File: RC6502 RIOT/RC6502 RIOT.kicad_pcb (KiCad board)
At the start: 2 copper layers, 99.1 x 69.2 mm, 45 parts, among them J1 Audio, J2 VDU_BASE, J3 P, J8 Composite, J9 RC6502_Backplane_Extra, U1 TIA_NTSC, U2 74HCT138, U3 VDU_Port, X1 3.579545 MHz

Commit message: RIOT module layout done
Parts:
- removed C10, C9: 470pF, Capacitors_THT:C_Disc_D4.7mm_W2.5mm_P5.00mm
- removed C11: 820pF, Capacitors_THT:C_Disc_D4.7mm_W2.5mm_P5.00mm
- removed C12: 100nF, Capacitors_THT:C_Disc_D4.7mm_W2.5mm_P5.00mm
- removed C5, C6: 68nF, Capacitors_THT:C_Disc_D4.7mm_W2.5mm_P5.00mm
- removed C7: 22pF, Capacitors_THT:C_Disc_D4.7mm_W2.5mm_P5.00mm
- removed C8: 47pF, Capacitors_THT:C_Disc_D4.7mm_W2.5mm_P5.00mm
- removed J8: Composite, RCA:rca_yellow
- removed R10: 6k8, Resistors_THT:R_Axial_DIN0207_L6.3mm_D2.5mm_P10.16mm_Horizontal
- removed R11, R12, R9: 1k, Resistors_THT:R_Axial_DIN0207_L6.3mm_D2.5mm_P10.16mm_Horizontal
- removed R13: 18k, Resistors_THT:R_Axial_DIN0207_L6.3mm_D2.5mm_P10.16mm_Horizontal
- removed R14: 9k1, Resistors_THT:R_Axial_DIN0207_L6.3mm_D2.5mm_P10.16mm_Horizontal
- removed R15, R16: 220, Resistors_THT:R_Axial_DIN0207_L6.3mm_D2.5mm_P10.16mm_Horizontal
- removed R17, R18: 10k, Resistors_THT:R_Axial_DIN0207_L6.3mm_D2.5mm_P10.16mm_Horizontal
- removed R2, R4, R6, R8: 3K3, Resistors_THT:R_Axial_DIN0207_L6.3mm_D2.5mm_P10.16mm_Horizontal
- removed R3: 56k, Resistors_THT:R_Axial_DIN0207_L6.3mm_D2.5mm_P10.16mm_Horizontal
- removed R5: 27K, Resistors_THT:R_Axial_DIN0207_L6.3mm_D2.5mm_P10.16mm_Horizontal
- removed R7: 110k, Resistors_THT:R_Axial_DIN0207_L6.3mm_D2.5mm_P10.16mm_Horizontal
- removed RV1: 500k, Potentiometers:Potentiometer_Trimmer_Bourns_3296W
- removed U3: VDU_Port, vdu_amplifier:Amplifier
- removed X1: 3.579545 MHz, Oscillator:Oscillator_DIP-14
- added J4: RIGHT PLAYER, RND_DSUB:DSUB-9_Male_Vertical_Pitch2.77x2.84mm, F.Cu at (143.5, 128.9)
- added J5: AUX, Pin_Headers:Pin_Header_Straight_1x03_Pitch2.54mm, F.Cu at (54.6, 117.5)
- added JP10: R_DIFF, Pin_Headers:Pin_Header_Straight_1x03_Pitch2.54mm, F.Cu at (108.6, 76.8)
- added JP11: RAM_EN, Pin_Headers:Pin_Header_Straight_1x03_Pitch2.54mm, F.Cu at (108.6, 121.3)
- added JP6: RAM_SEL, Pin_Headers:Pin_Header_Straight_1x03_Pitch2.54mm, F.Cu at (108.6, 132.7)
- added JP7: IRQ_SEL, Pin_Headers:Pin_Header_Straight_1x03_Pitch2.54mm, F.Cu at (95.9, 121.3)
- added JP8: B/W, Pin_Headers:Pin_Header_Straight_1x03_Pitch2.54mm, F.Cu at (84.5, 76.8)
- added JP9: L_DIFF, Pin_Headers:Pin_Header_Straight_1x03_Pitch2.54mm, F.Cu at (96.5, 76.8)
- added SW1: SELECT, Buttons_Switches_THT:SW_PUSH_6mm, F.Cu at (117.5, 76.8)
- added SW2: START, Buttons_Switches_THT:SW_PUSH_6mm, F.Cu at (128.3, 76.8)
- C3, C4: value 68nF -> 1nF
- J1: value Audio -> LEFT PLAYER; footprint RCA:rca_yellow -> RND_DSUB:DSUB-9_Male_Vertical_Pitch2.77x2.84mm
- J3: value P -> Analog
- JP1: value CADJ -> IRQ_EN; footprint Pin_Headers:Pin_Header_Straight_1x02_Pitch2.54mm -> Pin_Headers:Pin_Header_Straight_1x03_Pitch2.54mm
- JP2: value CS0_SEL -> CS1_SEL
- JP3: value CS3_SEL -> CS2_SEL
- R1: value 27k -> 3k3
- U1: value TIA_NTSC -> RIOT
- moved JP4 64.7 mm to (70.5, 138.4), turned to 90 degrees
- moved JP5 64.5 mm to (61.6, 138.4), turned to 90 degrees
- moved JP2 49.1 mm to (83.2, 132.7), turned to 90 degrees
- moved JP1 43.3 mm to (83.2, 121.3), turned to 90 degrees
- moved C4 40.6 mm to (54.6, 112.4)
- moved C3 35.9 mm to (54.6, 102.2)
- moved JP3 33.4 mm to (95.9, 132.7), turned to 90 degrees
- moved R1 21.6 mm to (103.5, 111.8), turned to 180 degrees
- moved J2 13.3 mm to (132.7, 117.5)
- moved C2 13.3 mm to (126.4, 111.1)
- moved U2 13.3 mm to (120.0, 114.9)
- moved J1 5.46 mm to (143.5, 96.5)
- moved J3 5.24 mm to (70.5, 76.8)
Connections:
- C3 pad 1: GND -> /PA0
- C3 pad 2: /P0 -> GND
- C4 pad 1: GND -> /PB0
- C4 pad 2: /P1 -> GND
- J1 pad 1: GND -> /PA4
- J1 pad 2: Net-(J1-Pad2) -> /PA5
- J2 pad 10: TIA_BASE -> RIOT_BASE
- J2 pad 12: TIA_BASE -> RIOT_BASE
- J2 pad 14: TIA_BASE -> RIOT_BASE
- J2 pad 2: TIA_BASE -> RIOT_BASE
- J2 pad 4: TIA_BASE -> RIOT_BASE
- J2 pad 6: TIA_BASE -> RIOT_BASE
- J2 pad 8: TIA_BASE -> RIOT_BASE
- J9 pad 10: (no net) -> /A6
- J9 pad 20: (no net) -> /~RES
- J9 pad 21: /PHI0 -> (no net)
- J9 pad 22: (no net) -> /IRQ_IN
- J9 pad 25: /RDY -> (no net)
- J9 pad 37: (no net) -> /NMI_IN
- J9 pad 5: (no net) -> /A11
- J9 pad 7: (no net) -> /A9
- JP1 pad 2: /CADJ -> /~IRQ
- JP2 pad 1: /A12 -> /A7
- JP2 pad 2: /~CS0 -> /CS1
- JP2 pad 3: TIA_BASE -> VCC
- JP3 pad 1: /A7 -> /A12
- JP3 pad 2: /~CS3 -> /~CS2
- JP3 pad 3: GND -> RIOT_BASE
- JP4 pad 1: /T1_IN -> /T1
- JP5 pad 1: /T0_IN -> /T0
- R1 pad 1: /CSYNC -> VCC
- R1 pad 2: VIDEO -> Net-(JP1-Pad1)
- U1 pad 10: /CADJ -> /PA2
- U1 pad 11: /OSC_IN -> /PA3
- U1 pad 12: /AUD0 -> /PA4
- U1 pad 13: /AUD0 -> /PA5
- U1 pad 14: /D0 -> /PA6
- U1 pad 15: /D1 -> /PA7
- U1 pad 16: /D2 -> /PB7
- U1 pad 17: /D3 -> /PB6
- U1 pad 18: /D4 -> /PB5
- U1 pad 19: /D5 -> /PB4
- U1 pad 2: /CSYNC -> /A5
- U1 pad 21: /~CS3 -> /PB3
- U1 pad 22: GND -> /PB2
- U1 pad 23: VCC -> /PB1
- U1 pad 24: /~CS0 -> /PB0
- U1 pad 25: /R/~W -> /~IRQ
- U1 pad 26: /PHI2 -> /D7
- U1 pad 27: /A5 -> /D6
- U1 pad 28: /A4 -> /D5
- U1 pad 29: /A3 -> /D4
- U1 pad 3: /RDY -> /A4
- U1 pad 30: /A2 -> /D3
- U1 pad 31: /A1 -> /D2
- U1 pad 32: /A0 -> /D1
- U1 pad 33: /D6 -> /D0
- U1 pad 34: /D7 -> /~RES
- U1 pad 35: /T1 -> /R/~W
- U1 pad 36: /T0 -> /~RS
- U1 pad 37: /P3 -> /~CS2
- U1 pad 38: /P2 -> /CS1
- U1 pad 39: /P1 -> /PHI2
- U1 pad 4: /PHI0 -> /A3
- U1 pad 40: /P0 -> /A6
- U1 pad 5: /LUM1 -> /A2
- U1 pad 6: (no net) -> /A1
- U1 pad 7: /LUM2 -> /A0
- U1 pad 8: /LUM0 -> /PA0
- U1 pad 9: /COLOR -> /PA1
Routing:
- net VCC: track 470.4 -> 245.1 mm, vias 10 -> 5
- net /PB0: track 0.00 -> 137.5 mm, vias 0 -> 2
- net /A6: track 0.00 -> 126.6 mm, vias 0 -> 4
- net /PA0: track 0.00 -> 113.3 mm, vias 0 -> 3
- net /PA7: track 0.00 -> 112.9 mm, vias 0 -> 3
- net /PB1: track 0.00 -> 110.5 mm
- net /PA6: track 0.00 -> 108.1 mm, vias 0 -> 3
- net /PA1: track 0.00 -> 106.1 mm, vias 0 -> 3
- net /PA2: track 0.00 -> 105.2 mm, vias 0 -> 3
- net /P1: track 22.2 -> 126.7 mm, vias 0 -> 2
- net /PA3: track 0.00 -> 103.9 mm, vias 0 -> 1
- net /PA5: track 0.00 -> 103.6 mm, vias 0 -> 3
- net /P0: track 20.5 -> 123.7 mm, vias 0 -> 2
- net /PA4: track 0.00 -> 98.5 mm, vias 0 -> 1
- net Net-(J9-Pad38): track 106.8 -> 10.6 mm, vias 4 -> 0
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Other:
- outline, holes or cut-outs redrawn
- board text added: "$80 $280"
- board text added: "$ADR"
- board text added: "+ $0 + $1 + $2 + $3 + $4 + $14 + $15 + $16 + $17"
- board text added: "1-2 Disabled 2-3 Enabled"
- board text added: "1-2 ~IRQ 2-3 ~NMI"
- board text added: "6532"
- board text added: "Atari 2600"
- board text added: "B/W COLOR"
- board text added: "BASE"
- board text added: "CS1"
- board text added: "Description"
- board text added: "IRQ_EN"
- board text added: "IRQ_SEL"
- board text added: "LEFT DIFFICULTY"
- board text added: "Port A data register (joysticks...) Port A data direction register (DDR) Port B data (console switches) Port B DDR Timer output Set 1 clock interval Set 8 clock interval Set 64 clock interval Set 1024 clock interval"
- board text added: "RAM I/O TIMER (RIOT) 6532"
- board text added: "RAM Registers"
- board text added: "RC6502"
- board text added: "RC6502 RIOT 2600 Revision A"
- board text added: "RIGHT DIFFICULTY"
- board text added: "RIOT BASE"
- board text added: "RIOT_BASE RIOT_BASE + $800"
- board text added: "Swcha Swacnt Swchb Swbcnt Intim Tim1t Tim8t Tim64t T1024t"
- board text added: "Symbol"
- board text added: "~CS2"
- board text added: "~RAM_EN"
- board text added: "~RAM_SEL"
- board text removed: "2x 470pF"
- board text removed: "2x 68nF"
- board text removed: "3.579545 MHz"
- board text removed: "ANALOG INPUT"
- board text removed: "AUDIO"
- board text removed: "BUS EN"
- board text removed: "CO10444"
- board text removed: "COLOR DELAY ADJUST"
- board text removed: "Composite Video Amplifier"
- board text removed: "NTSC Oscillator"
- board text removed: "RC6502 TIA (NTSC) Revision A"
- board text removed: "T0"
- board text removed: "T1"
- board text removed: "Television Interface Adapter (TIA) CO10444"
- board text removed: "VDU BASE"
- board text removed: "VIDEO"
- board text removed: "~CS0"
- board text removed: "~CS3"

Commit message: Updated gerbers for order
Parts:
- moved J3 5.08 mm to (75.6, 76.8)
- moved JP8 1.27 mm to (83.2, 76.8)
- moved SW1 0.64 mm to (118.1, 76.8)
- moved JP9 0.63 mm to (95.9, 76.8)
- moved SW2 0.63 mm to (128.9, 76.8)
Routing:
- net /P3: track 90.2 -> 85.1 mm
- net /P2: track 83.9 -> 78.8 mm
- net /P1: track 126.7 -> 121.6 mm
- net /P0: track 123.7 -> 118.6 mm
- net /PB0: track 137.5 -> 139.2 mm
- net /PB1: track 110.5 -> 111.8 mm
- net /PB3: track 83.9 -> 82.6 mm
- net /PB6: track 85.4 -> 84.8 mm
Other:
- board text added: "T0"
- board text added: "T1"

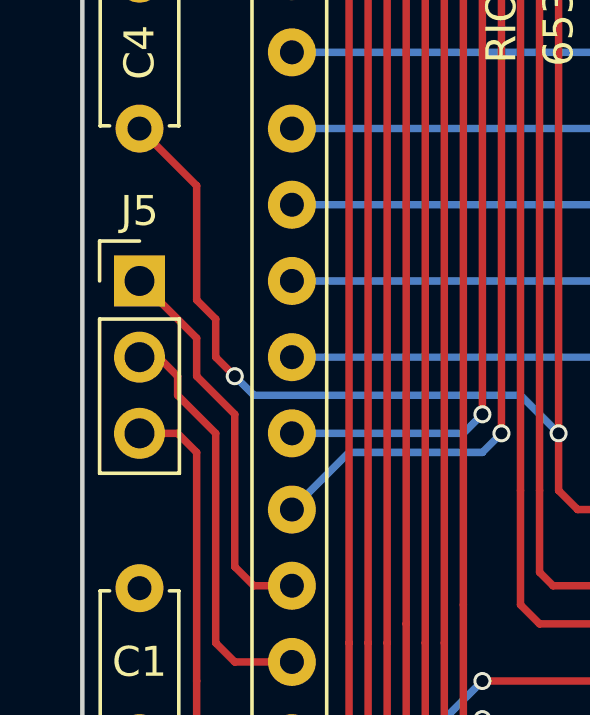
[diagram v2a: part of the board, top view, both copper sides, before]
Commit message: Added silkscreen markings for AUX header
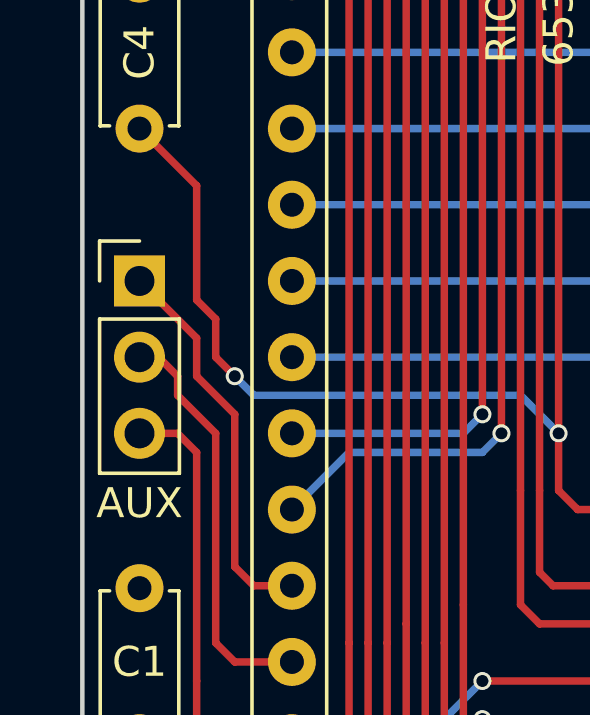
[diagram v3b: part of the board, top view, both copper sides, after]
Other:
- board text added: "AUX"
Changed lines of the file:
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@@
     (links 103)
     (no_connects 0)
-    (area 49.19 44.45 153.84 156.924763)
+    (area 52.629999 74.854999 151.840001 144.220001)
     (thickness 1.6)
-    (drawings 139)
+    (drawings 143)
     (tracks 1120)
     (zones 0)
@@
     (descr "Through hole straight pin header, 1x03, 2.54mm pitch, single row")
     (tags "Through hole pin header THT 1x03 2.54mm single row")
-    (fp_text reference J5 (at 0 -2.33) (layer F.SilkS)
-      (effects (font (size 1 1) (thickness 0.15)))
-    )
-    (fp_text value AUX (at 0 7.41) (layer F.Fab)
+    (fp_text reference J5 (at 0 -2.33) (layer F.Fab)
+      (effects (font (size 1 1) (thickness 0.15)))
+    )
+    (fp_text value AUX (at 0 7.41) (layer F.SilkS)
       (effects (font (size 1 1) (thickness 0.15)))
     )
@@
     )
   )
+  (gr_text AUX (at 54.61 125.095) (layer B.SilkS)
+    (effects (font (size 1 1) (thickness 0.15)) (justify mirror))
+  )
+  (gr_line (start 56.515 115.57) (end 52.705 115.57) (angle 90) (layer B.SilkS) (width 0.2))
+  (gr_line (start 56.515 124.46) (end 56.515 115.57) (angle 90) (layer B.SilkS) (width 0.2))
+  (gr_line (start 52.705 124.46) (end 56.515 124.46) (angle 90) (layer B.SilkS) (width 0.2))
   (gr_text T1 (at 76.2 138.43 270) (layer B.SilkS)
     (effects (font (size 1 1) (thickness 0.15)) (justify mirror))
